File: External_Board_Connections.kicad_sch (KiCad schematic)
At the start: 15 parts, among them J10 Conn_01x02, J11 Conn_01x06, J12 Conn_01x02, J13 Conn_01x02, J14 Conn_01x02, J15 Conn_01x02, J19 Conn_01x01_Socket, J20 Conn_01x01_Socket, J21 Conn_01x01_Socket, J22 Conn_01x01_Socket, J6 Conn_02x04_Odd_Even, J7 Conn_02x04_Odd_Even, J8 Conn_02x04_Odd_Even, J9 Conn_02x04_Odd_Even

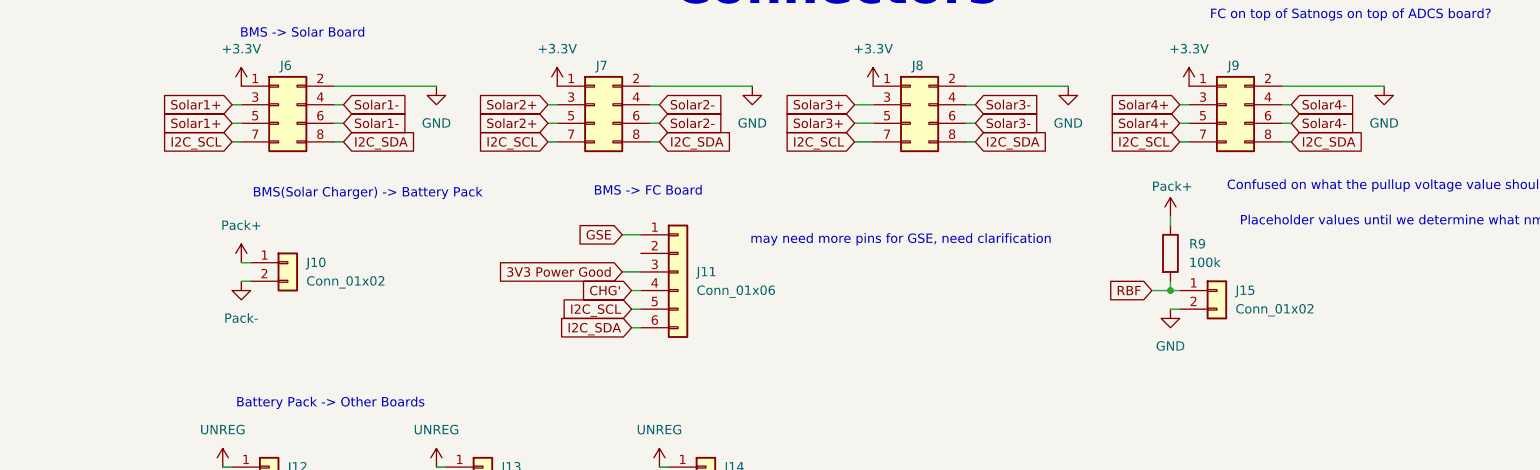
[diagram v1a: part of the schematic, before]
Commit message: I2C buffer Addtition
Added I2C compatible with hardware's component
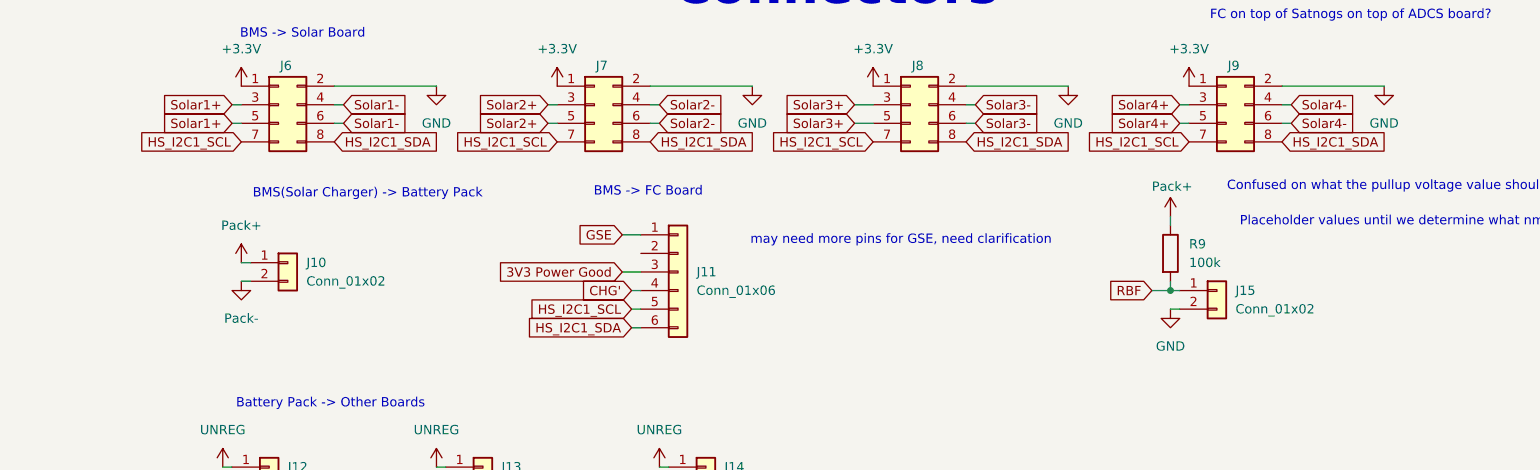
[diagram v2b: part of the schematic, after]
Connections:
- net I2C_SCL renamed HS_I2C1_SCL
- net I2C_SDA renamed HS_I2C1_SDA
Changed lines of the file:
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@@
-	(wire
-		(pts
-			(xy 77.47 123.19) (xy 78.74 123.19)
-		)
-		(stroke
-			(width 0)
-			(type default)
-		)
-	)
 	(wire
 		(pts
@@
 	(wire
 		(pts
-			(xy 135.89 123.19) (xy 134.62 123.19)
-		)
-		(stroke
-			(width 0)
-			(type default)
-		)
-	)
-	(wire
-		(pts
 			(xy 33.02 170.18) (xy 34.29 170.18)
 		)
@@
 	(wire
 		(pts
-			(xy 34.29 123.19) (xy 35.56 123.19)
-		)
-		(stroke
-			(width 0)
-			(type default)
-		)
-	)
-	(wire
-		(pts
 			(xy 53.34 41.91) (xy 53.34 46.99)
 		)
@@
 	(wire
 		(pts
-			(xy 49.53 123.19) (xy 48.26 123.19)
-		)
-		(stroke
-			(width 0)
-			(type default)
-		)
-	)
-	(wire
-		(pts
 			(xy 163.83 120.65) (xy 165.1 120.65)
 		)
@@
 	(wire
 		(pts
-			(xy 92.71 123.19) (xy 91.44 123.19)
-		)
-		(stroke
-			(width 0)
-			(type default)
-		)
-	)
-	(wire
-		(pts
 			(xy 62.23 170.18) (xy 63.5 170.18)
 		)
@@
 	(wire
 		(pts
-			(xy 163.83 123.19) (xy 165.1 123.19)
-		)
-		(stroke
-			(width 0)
-			(type default)
-		)
-	)
-	(wire
-		(pts
 			(xy 92.71 120.65) (xy 91.44 120.65)
 		)
@@
 	(wire
 		(pts
-			(xy 119.38 123.19) (xy 121.92 123.19)
-		)
-		(stroke
-			(width 0)
-			(type default)
-		)
-	)
-	(wire
-		(pts
 			(xy 91.44 115.57) (xy 105.41 115.57)
 		)
@@
 	(wire
 		(pts
-			(xy 179.07 123.19) (xy 177.8 123.19)
-		)
-		(stroke
-			(width 0)
-			(type default)
-		)
-	)
-	(wire
-		(pts
 			(xy 53.34 46.99) (xy 58.42 46.99)
 		)
@@
 		)
 	)
-	(global_label "I2C_SCL"
-		(shape input)
-		(at 77.47 123.19 180)
-		(fields_autoplaced yes)
-		(effects
-			(font
-				(size 1.27 1.27)
-			)
-			(justify right)
-		)
-		(property "Intersheetrefs" "${INTERSHEET_REFS}"
-			(at 66.9253 123.19 0)
+	(global_label "HS_I2C1_SCL"
+		(shape input)
+		(at 78.74 123.19 180)
+		(fields_autoplaced yes)
+		(effects
+			(font
+				(size 1.27 1.27)
+			)
+			(justify right)
+		)
+		(property "Intersheetrefs" "${INTERSHEET_REFS}"
+			(at 63.4782 123.19 0)
 			(hide yes)
 			(show_name no)
@@
 		)
 	)
-	(global_label "I2C_SDA"
-		(shape input)
-		(at 135.89 123.19 0)
-		(fields_autoplaced yes)
-		(effects
-			(font
-				(size 1.27 1.27)
-			)
-			(justify left)
-		)
-		(property "Intersheetrefs" "${INTERSHEET_REFS}"
-			(at 146.4952 123.19 0)
+	(global_label "HS_I2C1_SDA"
+		(shape input)
+		(at 134.62 123.19 0)
+		(fields_autoplaced yes)
+		(effects
+			(font
+				(size 1.27 1.27)
+			)
+			(justify left)
+		)
+		(property "Intersheetrefs" "${INTERSHEET_REFS}"
+			(at 149.9423 123.19 0)
 			(hide yes)
 			(show_name no)
@@
 		)
 	)
-	(global_label "I2C_SCL"
-		(shape input)
-		(at 34.29 123.19 180)
-		(fields_autoplaced yes)
-		(effects
-			(font
-				(size 1.27 1.27)
-			)
-			(justify right)
-		)
-		(property "Intersheetrefs" "${INTERSHEET_REFS}"
-			(at 23.7453 123.19 0)
+	(global_label "HS_I2C1_SCL"
+		(shape input)
+		(at 35.56 123.19 180)
+		(fields_autoplaced yes)
+		(effects
+			(font
+				(size 1.27 1.27)
+			)
+			(justify right)
+		)
+		(property "Intersheetrefs" "${INTERSHEET_REFS}"
+			(at 20.2982 123.19 0)
 			(hide yes)
 			(show_name no)
@@
 		)
 	)
-	(global_label "I2C_SCL"
-		(shape input)
-		(at 119.38 123.19 180)
-		(fields_autoplaced yes)
-		(effects
-			(font
-				(size 1.27 1.27)
-			)
-			(justify right)
-		)
-		(property "Intersheetrefs" "${INTERSHEET_REFS}"
-			(at 108.8353 123.19 0)
-			(hide yes)
-			(show_name no)
-			(do_not_autoplace no)
-			(effects
-				(font
-					(size 1.27 1.27)
-				)
-				(justify right)
-			)
-		)
-	)
-	(global_label "I2C_SDA"
-		(shape input)
-		(at 49.53 123.19 0)
-		(fields_autoplaced yes)
-		(effects
-			(font
-				(size 1.27 1.27)
-			)
-			(justify left)
-		)
-		(property "Intersheetrefs" "${INTERSHEET_REFS}"
-			(at 60.1352 123.19 0)
+	(global_label "HS_I2C1_SCL"
+		(shape input)
+		(at 121.92 123.19 180)
+		(fields_autoplaced yes)
+		(effects
+			(font
+				(size 1.27 1.27)
+			)
+			(justify right)
+		)
+		(property "Intersheetrefs" "${INTERSHEET_REFS}"
+			(at 106.6582 123.19 0)
+			(hide yes)
+			(show_name no)
+			(do_not_autoplace no)
+			(effects
+				(font
+					(size 1.27 1.27)
+				)
+				(justify right)
+			)
+		)
+	)
+	(global_label "HS_I2C1_SDA"
+		(shape input)
+		(at 48.26 123.19 0)
+		(fields_autoplaced yes)
+		(effects
+			(font
+				(size 1.27 1.27)
+			)
+			(justify left)
+		)
+		(property "Intersheetrefs" "${INTERSHEET_REFS}"
+			(at 63.5823 123.19 0)
 			(hide yes)
 			(show_name no)
@@
 		)
 	)
-	(global_label "I2C_SDA"
+	(global_label "HS_I2C1_SDA"
 		(shape input)
 		(at 88.9 148.59 180)
@@
 		)
 		(property "Intersheetrefs" "${INTERSHEET_REFS}"
-			(at 78.2948 148.59 0)
-			(hide yes)
-			(show_name no)
-			(do_not_autoplace no)
-			(effects
-				(font
-					(size 1.27 1.27)
-				)
-				(justify right)
-			)
-		)
-	)
-	(global_label "I2C_SDA"
-		(shape input)
-		(at 92.71 123.19 0)
-		(fields_autoplaced yes)
-		(effects
-			(font
-				(size 1.27 1.27)
-			)
-			(justify left)
-		)
-		(property "Intersheetrefs" "${INTERSHEET_REFS}"
-			(at 103.3152 123.19 0)
+			(at 73.5777 148.59 0)
+			(hide yes)
+			(show_name no)
+			(do_not_autoplace no)
+			(effects
+				(font
+					(size 1.27 1.27)
+				)
+				(justify right)
+			)
+		)
+	)
+	(global_label "HS_I2C1_SDA"
+		(shape input)
+		(at 91.44 123.19 0)
+		(fields_autoplaced yes)
+		(effects
+			(font
+				(size 1.27 1.27)
+			)
+			(justify left)
+		)
+		(property "Intersheetrefs" "${INTERSHEET_REFS}"
+			(at 106.7623 123.19 0)
 			(hide yes)
 			(show_name no)
@@
 		)
 	)
-	(global_label "I2C_SCL"
-		(shape input)
-		(at 163.83 123.19 180)
-		(fields_autoplaced yes)
-		(effects
-			(font
-				(size 1.27 1.27)
-			)
-			(justify right)
-		)
-		(property "Intersheetrefs" "${INTERSHEET_REFS}"
-			(at 153.2853 123.19 0)
-			(hide yes)
-			(show_name no)
-			(do_not_autoplace no)
-			(effects
-				(font
-					(size 1.27 1.27)
-				)
-				(justify right)
-			)
-		)
-	)
-	(global_label "I2C_SDA"
-		(shape input)
-		(at 179.07 123.19 0)
-		(fields_autoplaced yes)
-		(effects
-			(font
-				(size 1.27 1.27)
-			)
-			(justify left)
-		)
-		(property "Intersheetrefs" "${INTERSHEET_REFS}"
-			(at 189.6752 123.19 0)
+	(global_label "HS_I2C1_SCL"
+		(shape input)
+		(at 165.1 123.19 180)
+		(fields_autoplaced yes)
+		(effects
+			(font
+				(size 1.27 1.27)
+			)
+			(justify right)
+		)
+		(property "Intersheetrefs" "${INTERSHEET_REFS}"
+			(at 149.8382 123.19 0)
+			(hide yes)
+			(show_name no)
+			(do_not_autoplace no)
+			(effects
+				(font
+					(size 1.27 1.27)
+				)
+				(justify right)
+			)
+		)
+	)
+	(global_label "HS_I2C1_SDA"
+		(shape input)
+		(at 177.8 123.19 0)
+		(fields_autoplaced yes)
+		(effects
+			(font
+				(size 1.27 1.27)
+			)
+			(justify left)
+		)
+		(property "Intersheetrefs" "${INTERSHEET_REFS}"
+			(at 193.1223 123.19 0)
 			(hide yes)
 			(show_name no)
@@
 		)
 	)
-	(global_label "I2C_SCL"
+	(global_label "HS_I2C1_SCL"
 		(shape input)
 		(at 88.9 146.05 180)
@@
 		)
 		(property "Intersheetrefs" "${INTERSHEET_REFS}"
-			(at 78.3553 146.05 0)
-			(hide yes)
-			(show_name no)
+			(at 73.6382 146.05 0)
+			(hide yes)
+			(show_name no)

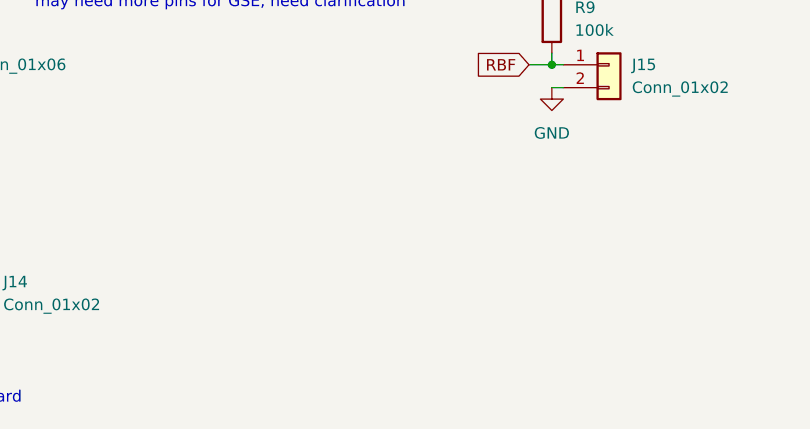
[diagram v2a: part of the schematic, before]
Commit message: Updates to connector and battery monitor
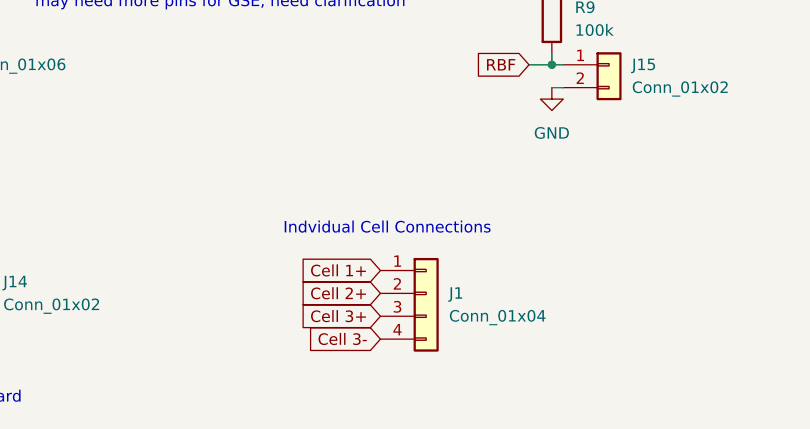
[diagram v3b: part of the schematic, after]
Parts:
- added J1: Conn_01x04, symbol Connector_Generic:Conn_01x04
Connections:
- new net Cell 1+: J1.1 (Pin_1)
- new net Cell 2+: J1.2 (Pin_2)
- new net Cell 3+: J1.3 (Pin_3)
- new net Cell 3-: J1.4 (Pin_4)
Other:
- note added: "Indvidual Cell Connections"
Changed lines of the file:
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@@
+		)
+	)
+	(text "Indvidual Cell Connections"
+		(exclude_from_sim no)
+		(at 144.272 161.798 0)
+		(effects
+			(font
+				(size 1.27 1.27)
+			)
 		)
 	)
@@
 		)
 	)
+	(global_label "Cell 3+"
+		(shape input)
+		(at 143.51 171.45 180)
+		(fields_autoplaced yes)
+		(effects
+			(font
+				(size 1.27 1.27)
+			)
+			(justify right)
+		)
+		(property "Intersheetrefs" "${INTERSHEET_REFS}"
+			(at 133.0863 171.45 0)
+			(hide yes)
+			(show_name no)
+			(do_not_autoplace no)
+			(effects
+				(font
+					(size 1.27 1.27)
+				)
+				(justify right)
+			)
+		)
+	)
 	(global_label "HS_I2C1_SDA"
 		(shape input)
@@
 		)
 	)
+	(global_label "Cell 1+"
+		(shape input)
+		(at 143.51 166.37 180)
+		(fields_autoplaced yes)
+		(effects
+			(font
+				(size 1.27 1.27)
+			)
+			(justify right)
+		)
+		(property "Intersheetrefs" "${INTERSHEET_REFS}"
+			(at 133.0863 166.37 0)
+			(hide yes)
+			(show_name no)
+			(do_not_autoplace no)
+			(effects
+				(font
+					(size 1.27 1.27)
+				)
+				(justify right)
+			)
+		)
+	)
 	(global_label "HS_I2C1_SDA"
 		(shape input)
@@
 		)
 	)
+	(global_label "Cell 3-"
+		(shape input)
+		(at 143.51 173.99 180)
+		(fields_autoplaced yes)
+		(effects
+			(font
+				(size 1.27 1.27)
+			)
+			(justify right)
+		)
+		(property "Intersheetrefs" "${INTERSHEET_REFS}"
+			(at 133.0863 173.99 0)
+			(hide yes)
+			(show_name no)
+			(do_not_autoplace no)
+			(effects
+				(font
+					(size 1.27 1.27)
+				)
+				(justify right)
+			)
+		)
+	)
 	(global_label "Solar2+"
 		(shape input)
@@
 				)
 				(justify left)
+			)
+		)
+	)
+	(global_label "Cell 2+"
+		(shape input)
+		(at 143.51 168.91 180)
+		(fields_autoplaced yes)
+		(effects
+			(font
+				(size 1.27 1.27)
+			)
+			(justify right)
+		)
+		(property "Intersheetrefs" "${INTERSHEET_REFS}"
+			(at 133.0863 168.91 0)
+			(hide yes)
+			(show_name no)
+			(do_not_autoplace no)
+			(effects
+				(font
+					(size 1.27 1.27)
+				)
+				(justify right)
 			)
 		)
@@
 					(unit 1)
 				)
+			)
+		)
+	)
+	(symbol
+		(lib_id "Connector_Generic:Conn_01x04")
+		(at 148.59 168.91 0)
+		(unit 1)
+		(body_style 1)
+		(exclude_from_sim no)
+		(in_bom yes)
+		(on_board yes)
+		(in_pos_files yes)
+		(dnp no)
+		(fields_autoplaced yes)
+		(property "Reference" "J1"
+			(at 151.13 168.9099 0)
+			(show_name no)
+			(do_not_autoplace no)
+			(effects
+				(font
+					(size 1.27 1.27)
+				)
+				(justify left)
+			)
+		)
+		(property "Value" "Conn_01x04"
+			(at 151.13 171.4499 0)
+			(show_name no)
+			(do_not_autoplace no)
+			(effects
+				(font
+					(size 1.27 1.27)
+				)
+				(justify left)
+			)
+		)
+		(property "Footprint" ""
+			(at 148.59 168.91 0)
+			(hide yes)
+			(show_name no)
+			(do_not_autoplace no)
+			(effects
+				(font
+					(size 1.27 1.27)
+				)
+			)
+		)
+		(property "Datasheet" ""
+			(at 148.59 168.91 0)
+			(hide yes)
+			(show_name no)
+			(do_not_autoplace no)
+			(effects
+				(font
+					(size 1.27 1.27)
+				)
+			)
+		)
+		(property "Description" "Generic connector, single row, 01x04, script generated (kicad-library-utils/schlib/autogen/connector/)"
+			(at 148.59 168.91 0)
+			(hide yes)
+			(show_name no)
+			(do_not_autoplace no)
+			(effects
+				(font
+					(size 1.27 1.27)
+				)
+			)
+		)
+		(pin "3"
+		)
+		(pin "4"
+		)
+		(pin "1"
+		)
+		(pin "2"
+		)
+		(instances
+			(project "BMS_Board_Prototype"
+				(path "/4ee99911-836b-4752-8a2d-327c8b28dc47/420608bc-a1a4-412d-a20e-6570cff27a90"
+					(reference "J1")
+					(unit 1)
+				)

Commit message: Inhibit
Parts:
- removed J13, J15: Conn_01x02, symbol Connector_Generic:Conn_01x02
- removed R9: 100k, symbol Device:R
- added J2: Conn_01x04, symbol Connector_Generic:Conn_01x04
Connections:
- net GSE is gone; now on net 3V3 Power Good: J11.1 (Pin_1)
- net +3.3V: now also J2.3 (Pin_3)
- net 3V3 Power Good: no longer J11.3 (Pin_3)
- net GND: now also J2.2 (Pin_2), J2.4 (Pin_4)
- net UNREG: now also J2.1 (Pin_1)
- net SHDN': now reaches J11.2 (Pin_2)
- new net FAULT': J11.3 (Pin_3)
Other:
- note added: "Will need connectors for feet switches and RBF"
- note removed: "Confused on what the pullup voltage value should be"
- note removed: "Placeholder values until we determine what nmos we will use"
- note removed: "may need more pins for GSE, need clarification"
